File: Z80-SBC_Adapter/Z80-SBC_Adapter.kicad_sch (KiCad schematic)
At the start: 4 parts, among them J1 Z80-MBC2 direct, J4 Mini-DIN-6, J7 Z80-MBC2 direct

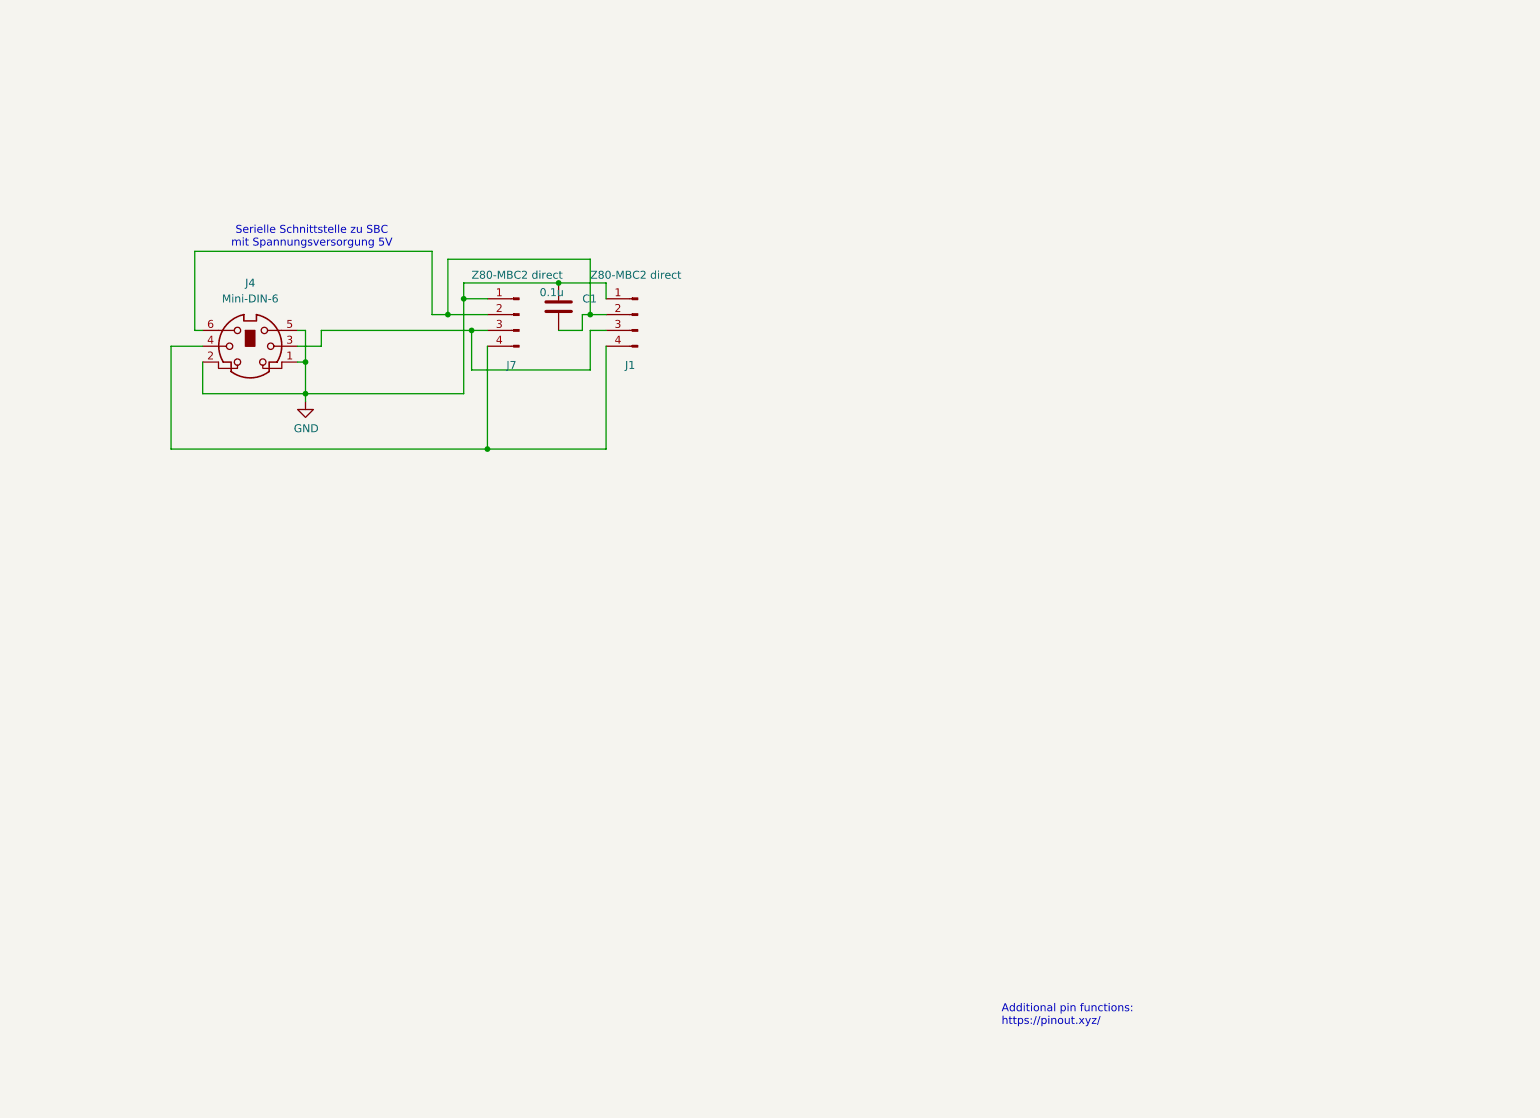
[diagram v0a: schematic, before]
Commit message: Geänderte Adapterplatine mit Readme
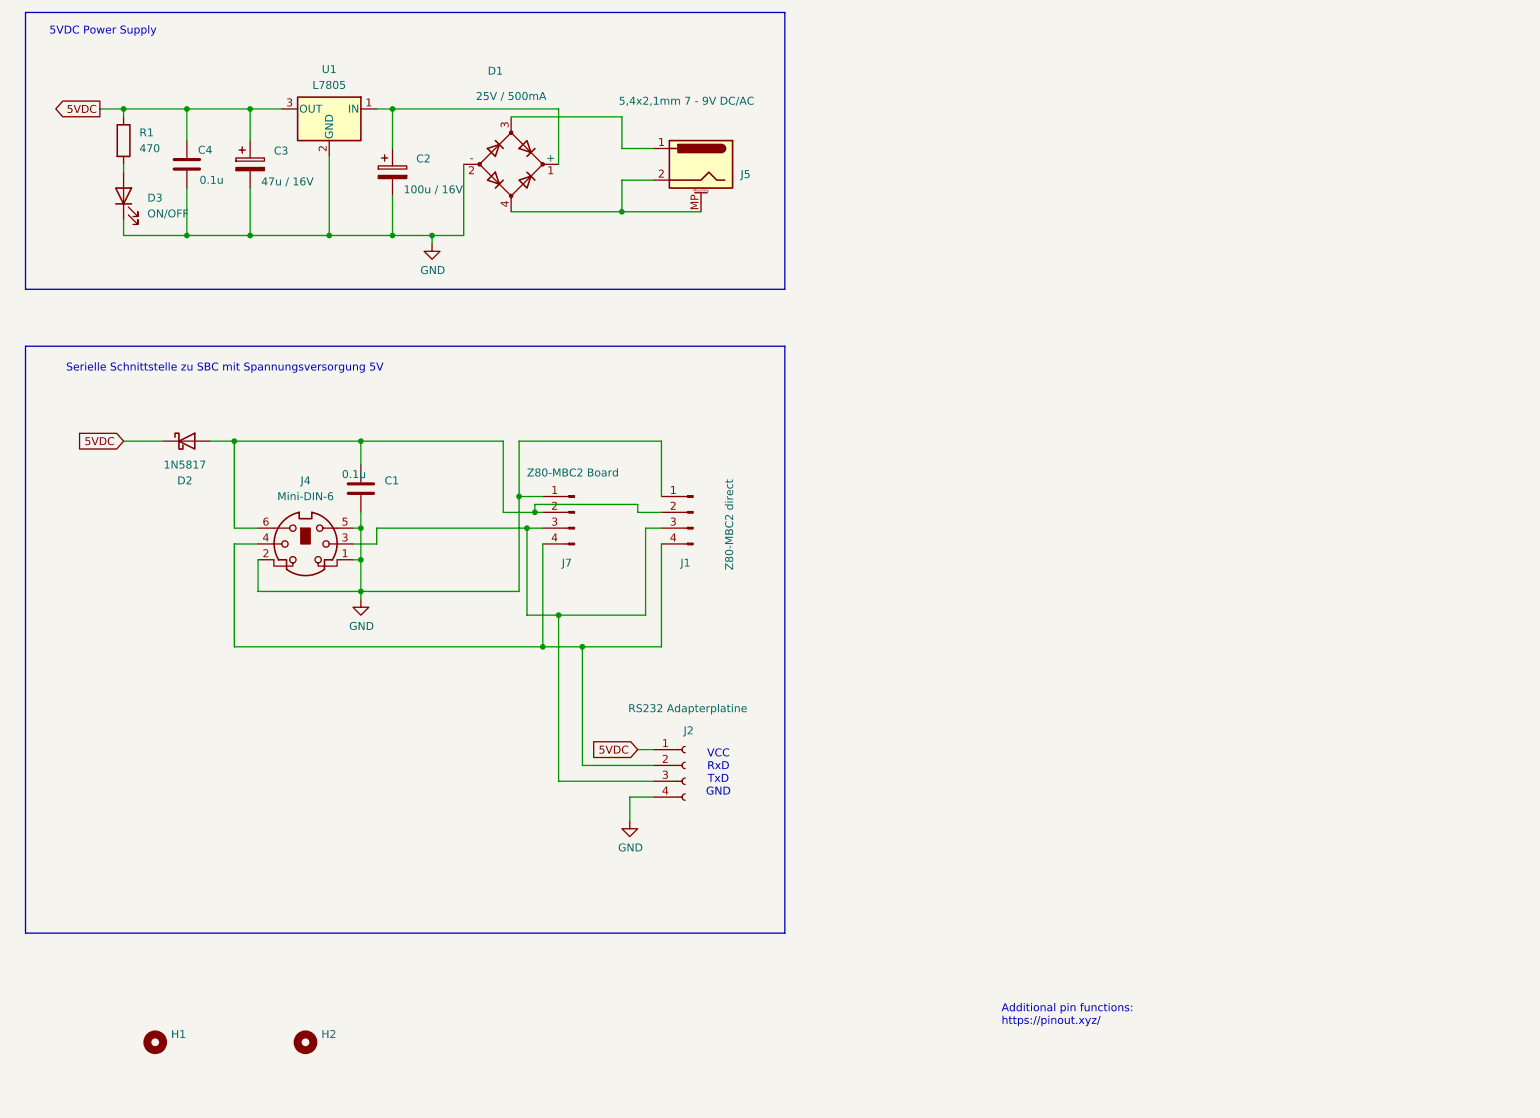
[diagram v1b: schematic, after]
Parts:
- added C2: 100u / 16V, Capacitor_THT:CP_Radial_D10.0mm_P5.00mm, symbol Device:C_Polarized
- added C3: 47u / 16V, Capacitor_THT:CP_Radial_D10.0mm_P5.00mm, symbol Device:C_Polarized
- added C4: 0.1u, Capacitor_THT:C_Rect_L7.0mm_W3.5mm_P5.00mm, symbol Device:C
- added D1: 25V / 500mA, Diode_THT:Diode_Bridge_Round_D8.9mm, symbol Device:D_Bridge_+-AA
- added D2: 1N5817, Diode_THT:D_DO-41_SOD81_P10.16mm_Horizontal, symbol Diode:1N5817
- added D3: ON/OFF, LED_THT:LED_D3.0mm, symbol Device:LED
- added H1, H2: MountingHole, MountingHole:MountingHole_3.2mm_M3, symbol Mechanical:MountingHole
- added J2: RS232 Adapterplatine, Connector_PinSocket_2.54mm:PinSocket_1x04_P2.54mm_Horizontal, symbol Connector:Conn_01x04_Socket
- added J5: 5,4x2,1mm 7 - 9V DC/AC, Connector_BarrelJack:BarrelJack_Wuerth_6941xx301002, symbol Connector:Barrel_Jack_MountingPin
- added R1: 470, Resistor_THT:R_Axial_DIN0207_L6.3mm_D2.5mm_P10.16mm_Horizontal, symbol Device:R
- added U1: L7805, Package_TO_SOT_THT:TO-220-3_Horizontal_TabDown, symbol Regulator_Linear:L7805
- J7: value Z80-MBC2 direct -> Z80-MBC2 Board
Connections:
- net GND: now also C1.2, C2.2, C3.2, C4.2, D1.2 (-), D3.1 (K), J2.4 (Pin_4), U1.2 (GND); no longer C1.1
- net at J1.2 (Pin_2), J4.6, J7.2 (Pin_2): now also C1.1, D2.2 (A); no longer C1.2
- net at J1.3 (Pin_3), J4.3, J7.3 (Pin_3): now also J2.3 (Pin_3)
- net at J1.4 (Pin_4), J4.4, J7.4 (Pin_4): now also J2.2 (Pin_2)
- new net: C2.1, D1.1 (+), U1.1 (IN)
- new net: D3.2 (A), R1.2
- new net: D1.3, J5.1
- new net: D1.4, J5.2, J5.MP (MountPin)
- new net 5VDC: C3.1, C4.1, D2.1 (K), J2.1 (Pin_1), R1.1, U1.3 (OUT)
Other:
- note added: "5VDC Power Supply"
- note added: "VCC RxD TxD GND"
- moved on the sheet: C1, J1, J4, J7

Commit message: Adapterplatine überarbeitet
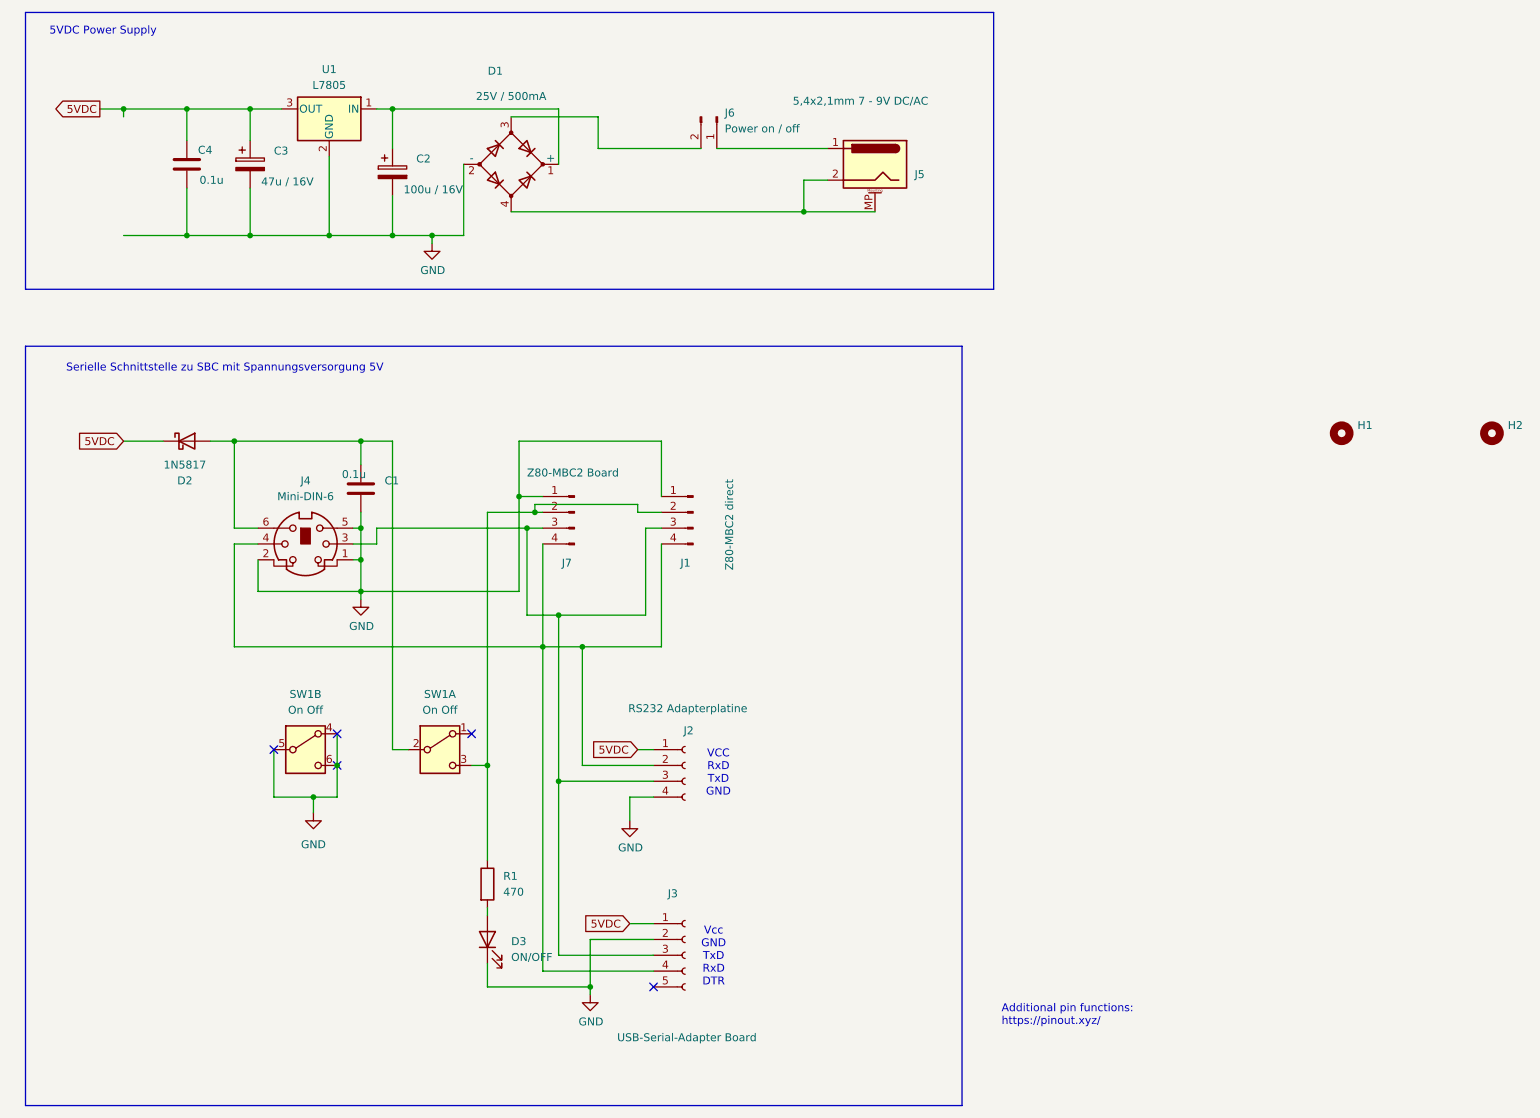
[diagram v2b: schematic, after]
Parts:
- added J3: USB-Serial-Adapter Board, Connector_PinSocket_2.54mm:PinSocket_1x05_P2.54mm_Vertical, symbol Connector:Conn_01x05_Socket
- added J6: Power on / off, Connector_PinHeader_2.54mm:PinHeader_1x02_P2.54mm_Vertical, symbol Connector:Conn_01x02_Pin
- added SW1: On Off, Button_Switch_THT:SW_CK_JS202011AQN_DPDT_Angled, symbol Switch:SW_DPDT_x2
- J2: footprint Connector_PinSocket_2.54mm:PinSocket_1x04_P2.54mm_Horizontal -> Connector_PinSocket_2.54mm:PinSocket_1x04_P2.54mm_Vertical
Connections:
- net 5VDC: now also J3.1 (Pin_1); no longer R1.1
- net GND: now also J3.2 (Pin_2), SW1.4 (A), SW1.5 (B), SW1.6 (C)
- net at C1.1, D2.2 (A), J4.6: now also SW1.2 (B); no longer J1.2 (Pin_2), J7.2 (Pin_2)
- net at J1.3 (Pin_3), J2.3 (Pin_3), J4.3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: now also J3.3 (Pin_3)
- net at J1.4 (Pin_4), J2.2 (Pin_2), J4.4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: now also J3.4 (Pin_4)
- net at J5.1: now also J6.1 (Pin_1); no longer D1.3
- new net: J1.2 (Pin_2), J7.2 (Pin_2), R1.1, SW1.3 (C)
- new net: D1.3, J6.2 (Pin_2)
- no-connect marks 0 -> 5
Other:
- note added: "Vcc GND TxD RxD DTR"
- moved on the sheet: D3, H1, H2, J5, R1
